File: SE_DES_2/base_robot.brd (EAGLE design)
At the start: 160 x 126.7 mm, 12 parts

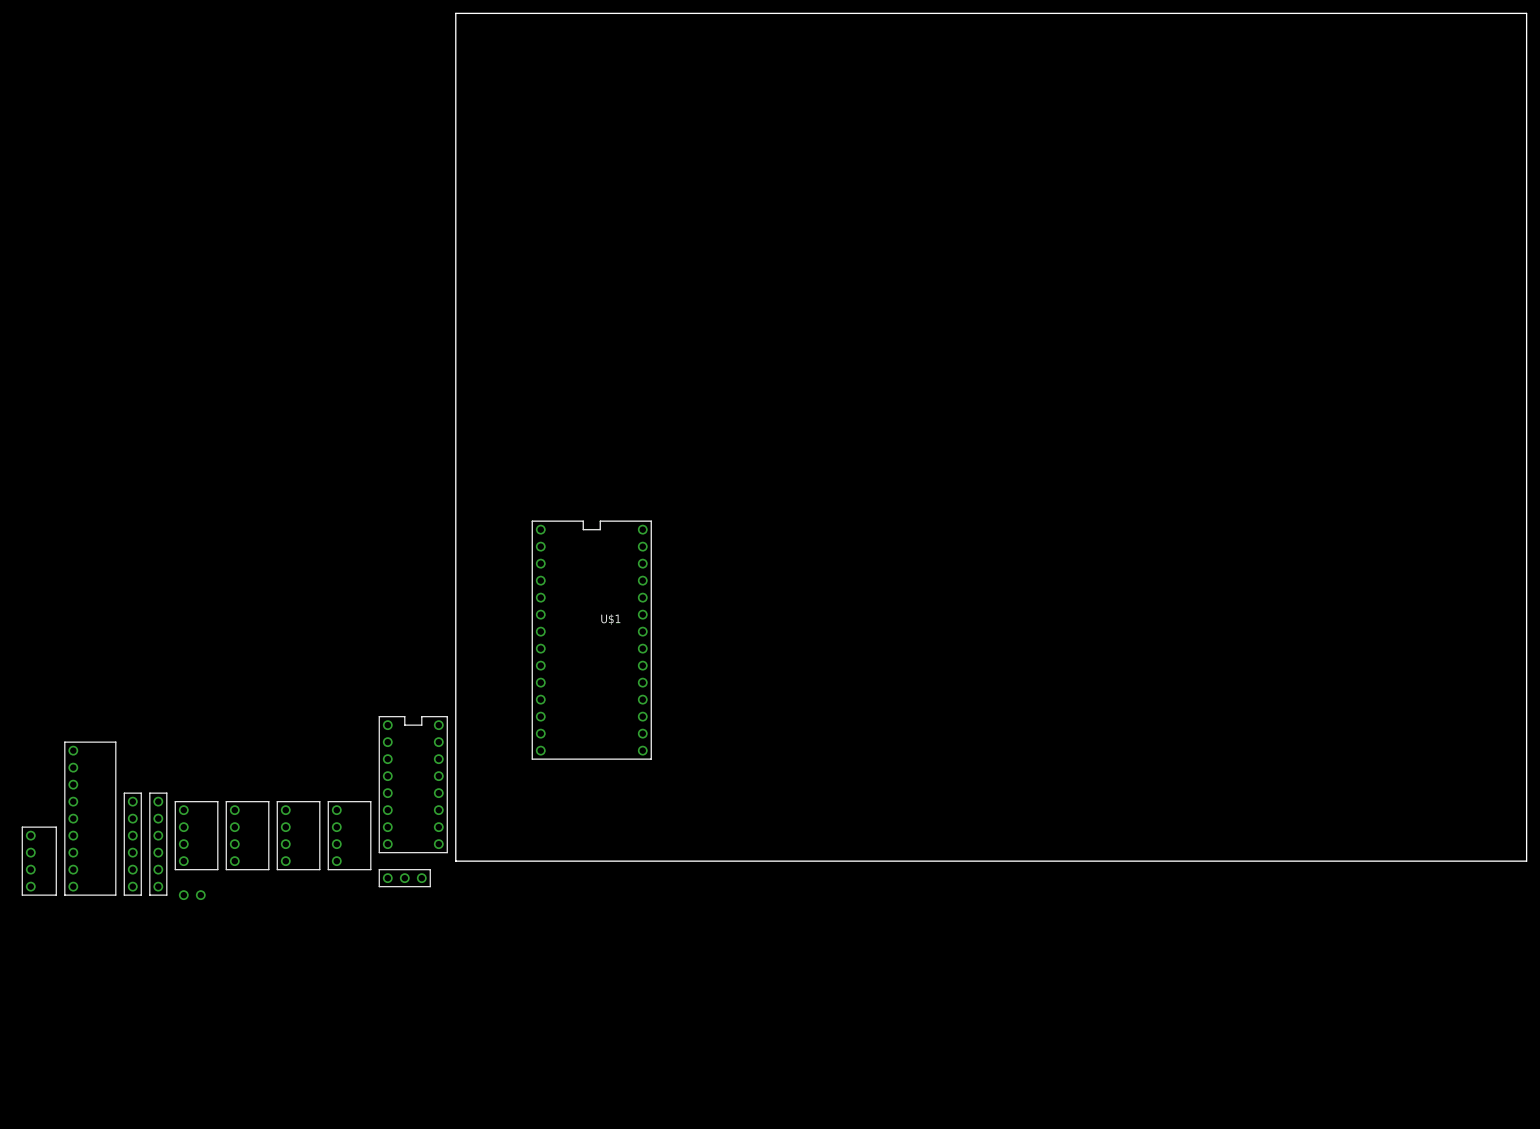
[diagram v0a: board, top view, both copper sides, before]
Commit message: pcb files for sen des se_des_2 is the latest one
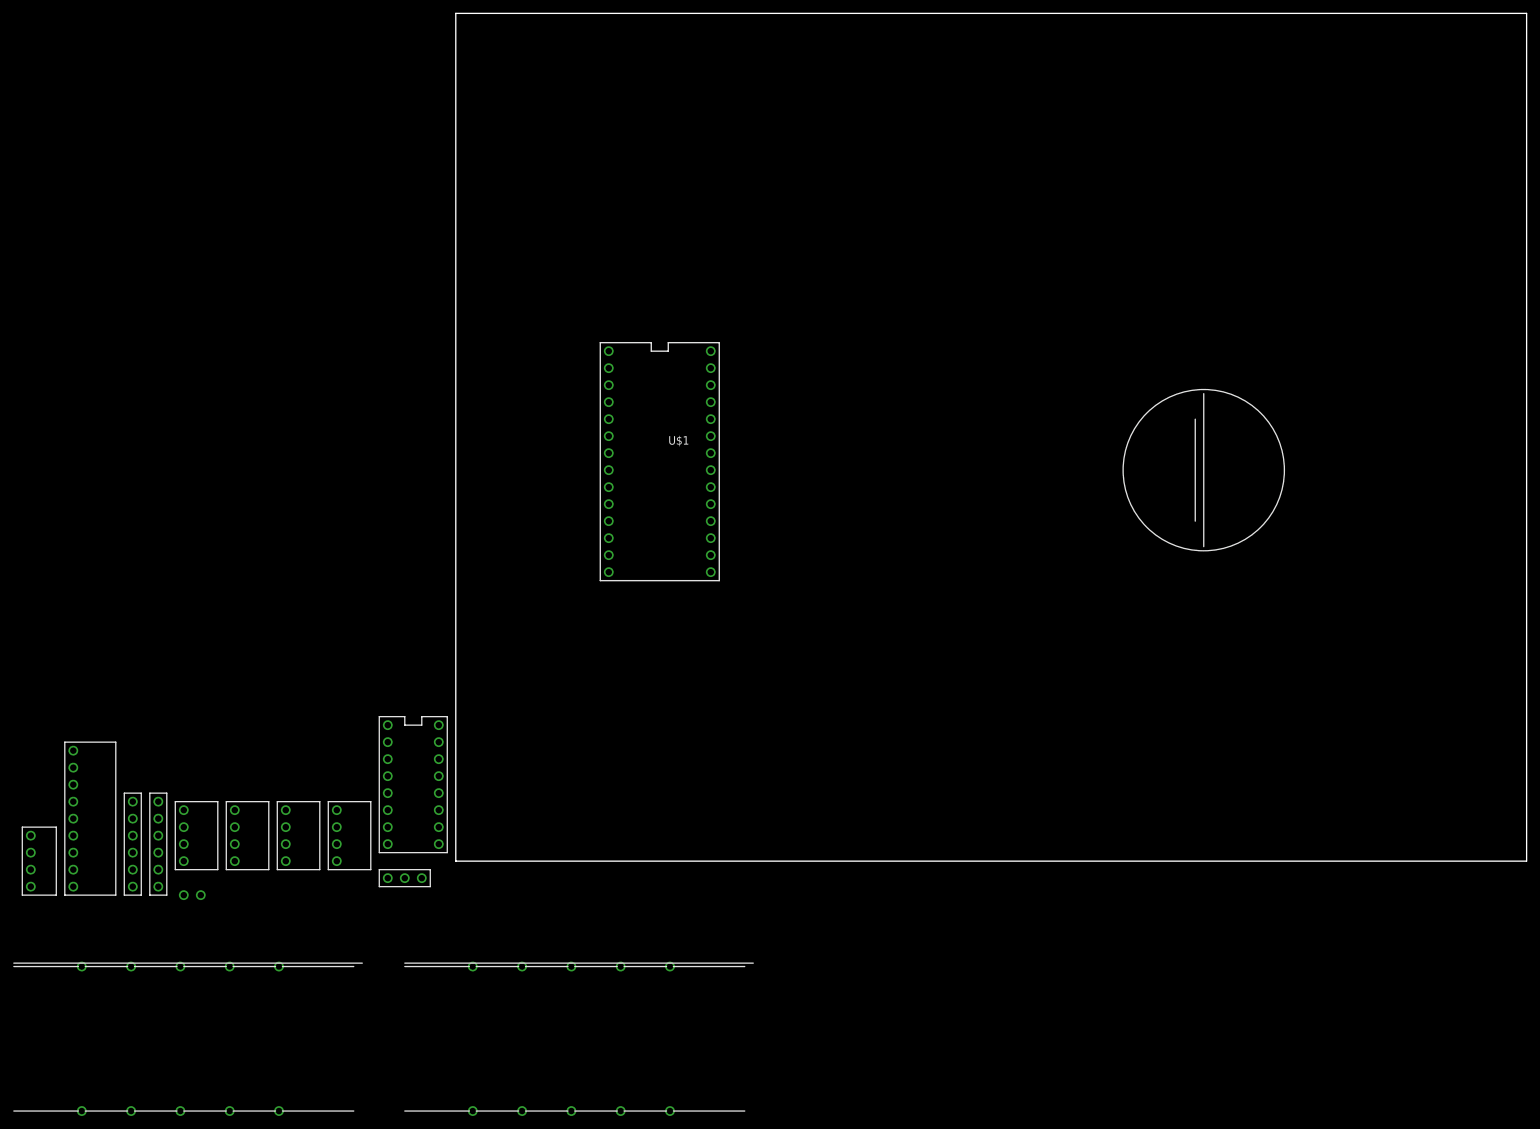
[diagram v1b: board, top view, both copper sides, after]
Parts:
- added U$13: 3_4_BALLCASTER, 3_4_BALLCASTER:3_4_BALLCASTER
- added U$14, U$15: MOTOR_BRACKET_25D, MOTOR_BRACKET_25D:MOTOR_BRACKET_25D
- moved U$1 28.5 mm to (30.5, 59.7)
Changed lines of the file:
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@@
 </autorouter>
 <elements>
-<element name="U$1" library="Teensy_3_and_LC_Series_Boards_v1.4" package="TEENSY_3.0-3.2&amp;LC_DIL" value="TEENSY_3.1-3.2_DIL" x="20.32" y="33.02" smashed="yes">
-<attribute name="NAME" x="21.59" y="35.56" size="1.27" layer="25" font="vector"/>
-<attribute name="VALUE" x="16.51" y="19.05" size="1.27" layer="27" font="vector"/>
+<element name="U$1" library="Teensy_3_and_LC_Series_Boards_v1.4" package="TEENSY_3.0-3.2&amp;LC_DIL" value="TEENSY_3.1-3.2_DIL" x="30.48" y="59.69" smashed="yes">
+<attribute name="NAME" x="31.75" y="62.23" size="1.27" layer="25" font="vector"/>
+<attribute name="VALUE" x="26.67" y="45.72" size="1.27" layer="27" font="vector"/>
 </element>
 <element name="U$2" library="motor_driver" package="MOTOR_DRIVER" value="MOTOR_DRIVER" x="-6.35" y="13.97" smashed="yes"/>
@@
 <element name="U$11" library="IMU" package="IMU" value="IMU" x="-55.88" y="11.43" smashed="yes"/>
 <element name="U$12" library="HC05_BLUETOOTH" package="HC05_BLUETOOTH" value="HC05_BLUETOOTH" x="-62.23" y="0" smashed="yes"/>
+<element name="U$13" library="3_4_BALLCASTER" package="3_4_BALLCASTER" value="3_4_BALLCASTER" x="110.49" y="50.8" smashed="yes" rot="R90"/>
+<element name="U$14" library="MOTOR_BRACKET_25D" package="MOTOR_BRACKET_25D" value="MOTOR_BRACKET_25D" x="-52.07" y="-15.24" smashed="yes"/>
+<element name="U$15" library="MOTOR_BRACKET_25D" package="MOTOR_BRACKET_25D" value="MOTOR_BRACKET_25D" x="6.35" y="-15.24" smashed="yes"/>
 </elements>
 <signals>
@@
 <contactref element="U$11" pad="VIN"/>
 <contactref element="U$12" pad="VCC"/>
-<wire x1="-2.54" y1="20.32" x2="27.94" y2="49.53" width="0" layer="19" extent="1-1"/>
+<wire x1="-2.54" y1="20.32" x2="38.1" y2="76.2" width="0" layer="19" extent="1-1"/>
 <wire x1="-10.16" y1="2.54" x2="-2.54" y2="20.32" width="0" layer="19" extent="1-1"/>
 <wire x1="-10.16" y1="-2.54" x2="-10.16" y2="2.54" width="0" layer="19" extent="1-1"/>
@@
 <contactref element="U$4" pad="TRIG"/>
 <contactref element="U$1" pad="7"/>
-<wire x1="-17.78" y1="5.08" x2="12.7" y2="29.21" width="0" layer="19" extent="1-1"/>
+<wire x1="-17.78" y1="5.08" x2="22.86" y2="55.88" width="0" layer="19" extent="1-1"/>
 </signal>
 <signal name="ECHO_1_CONN">
 <contactref element="U$4" pad="ECHO"/>
 <contactref element="U$1" pad="8"/>
-<wire x1="-17.78" y1="2.54" x2="12.7" y2="26.67" width="0" layer="19" extent="1-1"/>
+<wire x1="-17.78" y1="2.54" x2="22.86" y2="53.34" width="0" layer="19" extent="1-1"/>
 </signal>
 <signal name="TRIG_2_CONN">
 <contactref element="U$5" pad="TRIG"/>
 <contactref element="U$1" pad="9"/>
-<wire x1="-25.4" y1="5.08" x2="12.7" y2="24.13" width="0" layer="19" extent="1-1"/>
+<wire x1="-25.4" y1="5.08" x2="22.86" y2="50.8" width="0" layer="19" extent="1-1"/>
 </signal>
 <signal name="ECHO_2_CONN">
 <contactref element="U$5" pad="ECHO"/>
 <contactref element="U$1" pad="10"/>
-<wire x1="-25.4" y1="2.54" x2="12.7" y2="21.59" width="0" layer="19" extent="1-1"/>
+<wire x1="-25.4" y1="2.54" x2="22.86" y2="48.26" width="0" layer="19" extent="1-1"/>
 </signal>
 <signal name="CMN_GND">
@@
 <wire x1="-2.54" y1="12.7" x2="-10.16" y2="12.7" width="0" layer="19" extent="1-1"/>
 <wire x1="-2.54" y1="10.16" x2="-2.54" y2="12.7" width="0" layer="19" extent="1-1"/>
-<wire x1="12.7" y1="49.53" x2="-2.54" y2="12.7" width="0" layer="19" extent="1-1"/>
+<wire x1="22.86" y1="76.2" x2="-2.54" y2="12.7" width="0" layer="19" extent="1-1"/>
 </signal>
 <signal name="TRIG_3_CONN">
 <contactref element="U$6" pad="TRIG"/>
 <contactref element="U$1" pad="11"/>
-<wire x1="-33.02" y1="5.08" x2="12.7" y2="19.05" width="0" layer="19" extent="1-1"/>
+<wire x1="-33.02" y1="5.08" x2="22.86" y2="45.72" width="0" layer="19" extent="1-1"/>
 </signal>
 <signal name="ECHO_3_CONN">
 <contactref element="U$6" pad="ECHO"/>
 <contactref element="U$1" pad="12"/>
-<wire x1="12.7" y1="16.51" x2="-33.02" y2="2.54" width="0" layer="19" extent="1-1"/>
+<wire x1="22.86" y1="43.18" x2="-33.02" y2="2.54" width="0" layer="19" extent="1-1"/>
 </signal>
 <signal name="TRIG_4_CONN">
 <contactref element="U$7" pad="TRIG"/>
 <contactref element="U$1" pad="13"/>
-<wire x1="-40.64" y1="5.08" x2="27.94" y2="16.51" width="0" layer="19" extent="1-1"/>
+<wire x1="-40.64" y1="5.08" x2="38.1" y2="43.18" width="0" layer="19" extent="1-1"/>
 </signal>
 <signal name="ECHO_4_CONN">
 <contactref element="U$7" pad="ECHO"/>
 <contactref element="U$1" pad="14/A0"/>
-<wire x1="-40.64" y1="2.54" x2="27.94" y2="19.05" width="0" layer="19" extent="1-1"/>
+<wire x1="-40.64" y1="2.54" x2="38.1" y2="45.72" width="0" layer="19" extent="1-1"/>
 </signal>
 <signal name="M2_EN_CONN">
 <contactref element="U$2" pad="M2_ENABLE"/>
 <contactref element="U$1" pad="21/A7"/>
-<wire x1="-2.54" y1="2.54" x2="27.94" y2="36.83" width="0" layer="19" extent="1-1"/>
+<wire x1="-2.54" y1="2.54" x2="38.1" y2="63.5" width="0" layer="19" extent="1-1"/>
 </signal>
 <signal name="M1_EN_CONN">
 <contactref element="U$2" pad="M1_ENABLE"/>
 <contactref element="U$1" pad="20/A6"/>
-<wire x1="-10.16" y1="20.32" x2="27.94" y2="34.29" width="0" layer="19" extent="1-1"/>
+<wire x1="-10.16" y1="20.32" x2="38.1" y2="60.96" width="0" layer="19" extent="1-1"/>
 </signal>
 <signal name="L_M1_1">
@@
 <contactref element="U$1" pad="18/A4"/>
 <contactref element="U$11" pad="SDA"/>
-<wire x1="-57.15" y1="8.89" x2="27.94" y2="29.21" width="0" layer="19" extent="1-1"/>
+<wire x1="-57.15" y1="8.89" x2="38.1" y2="55.88" width="0" layer="19" extent="1-1"/>
 </signal>
 <signal name="SCL_CONN">
 <contactref element="U$1" pad="19/A5"/>
 <contactref element="U$11" pad="SCL"/>
-<wire x1="-57.15" y1="6.35" x2="27.94" y2="31.75" width="0" layer="19" extent="1-1"/>
+<wire x1="-57.15" y1="6.35" x2="38.1" y2="58.42" width="0" layer="19" extent="1-1"/>
 </signal>
 <signal name="TX_TO_RX">
 <contactref element="U$12" pad="RX"/>
 <contactref element="U$1" pad="1"/>
-<wire x1="12.7" y1="44.45" x2="-63.5" y2="3.81" width="0" layer="19" extent="1-1"/>
+<wire x1="22.86" y1="71.12" x2="-63.5" y2="3.81" width="0" layer="19" extent="1-1"/>
 </signal>
 <signal name="RX_TO_TX">
 <contactref element="U$12" pad="TX"/>
 <contactref element="U$1" pad="0"/>
-<wire x1="12.7" y1="46.99" x2="-63.5" y2="1.27" width="0" layer="19" extent="1-1"/>
+<wire x1="22.86" y1="73.66" x2="-63.5" y2="1.27" width="0" layer="19" extent="1-1"/>
 </signal>
 <signal name="M1_FWD_PWM_CONN">
 <contactref element="U$2" pad="M1_FWD_PWN"/>
 <contactref element="U$1" pad="3"/>
-<wire x1="-10.16" y1="17.78" x2="12.7" y2="39.37" width="0" layer="19" extent="1-1"/>
+<wire x1="-10.16" y1="17.78" x2="22.86" y2="66.04" width="0" layer="19" extent="1-1"/>
 </signal>
 <signal name="M1_REV_PWM_CONN">
 <contactref element="U$2" pad="M1_REV_PWN"/>
 <contactref element="U$1" pad="4"/>
-<wire x1="-10.16" y1="5.08" x2="12.7" y2="36.83" width="0" layer="19" extent="1-1"/>
+<wire x1="-10.16" y1="5.08" x2="22.86" y2="63.5" width="0" layer="19" extent="1-1"/>
 </signal>
 <signal name="M2_FWD_PWM_CONN">
 <contactref element="U$2" pad="M2_FWD_PWN"/>
 <contactref element="U$1" pad="5"/>
-<wire x1="-2.54" y1="5.08" x2="12.7" y2="34.29" width="0" layer="19" extent="1-1"/>
+<wire x1="-2.54" y1="5.08" x2="22.86" y2="60.96" width="0" layer="19" extent="1-1"/>
 </signal>
 <signal name="M2_REV_PWM_CONN">
 <contactref element="U$2" pad="M2_REV_PWM"/>
 <contactref element="U$1" pad="6"/>
-<wire x1="-2.54" y1="17.78" x2="12.7" y2="31.75" width="0" layer="19" extent="1-1"/>
+<wire x1="-2.54" y1="17.78" x2="22.86" y2="58.42" width="0" layer="19" extent="1-1"/>
 </signal>
 <signal name="OUTA_L_CONN">
 <contactref element="U$9" pad="OUTA"/>
 <contactref element="U$1" pad="15/A1"/>
-<wire x1="-44.45" y1="6.35" x2="27.94" y2="21.59" width="0" layer="19" extent="1-1"/>
+<wire x1="-44.45" y1="6.35" x2="38.1" y2="48.26" width="0" layer="19" extent="1-1"/>
 </signal>
 <signal name="OUTB_L_CONN">
 <contactref element="U$9" pad="OUTB"/>
 <contactref element="U$1" pad="2"/>
-<wire x1="-44.45" y1="8.89" x2="12.7" y2="41.91" width="0" layer="19" extent="1-1"/>
+<wire x1="-44.45" y1="8.89" x2="22.86" y2="68.58" width="0" layer="19" extent="1-1"/>
 </signal>
 <signal name="OUTA_R_CONN">
 <contactref element="U$10" pad="OUTA"/>
 <contactref element="U$1" pad="17/A3"/>
-<wire x1="-48.26" y1="6.35" x2="27.94" y2="26.67" width="0" layer="19" extent="1-1"/>
+<wire x1="-48.26" y1="6.35" x2="38.1" y2="53.34" width="0" layer="19" extent="1-1"/>
 </signal>
 <signal name="OUTB_R_CONN">
 <contactref element="U$10" pad="OUTB"/>
 <contactref element="U$1" pad="16/A2"/>
-<wire x1="-48.26" y1="8.89" x2="27.94" y2="24.13" width="0" layer="19" extent="1-1"/>
+<wire x1="-48.26" y1="8.89" x2="38.1" y2="50.8" width="0" layer="19" extent="1-1"/>
 </signal>
 </signals>
